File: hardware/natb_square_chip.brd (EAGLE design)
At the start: 13.5 x 13.5 mm, 8 parts, among them U1 TINY212, U2 MEGA32U4-MU

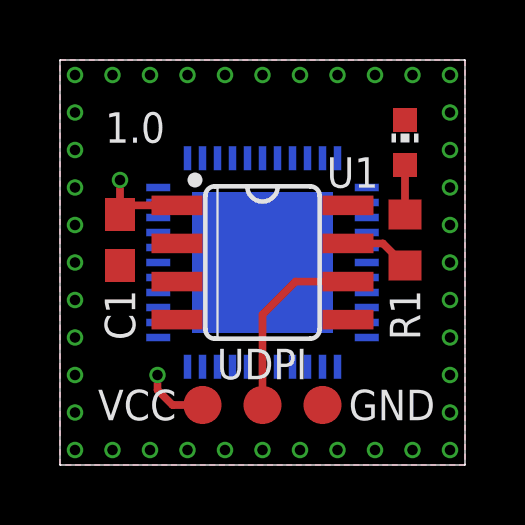
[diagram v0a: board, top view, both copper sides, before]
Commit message: Changes SOIC and BGA
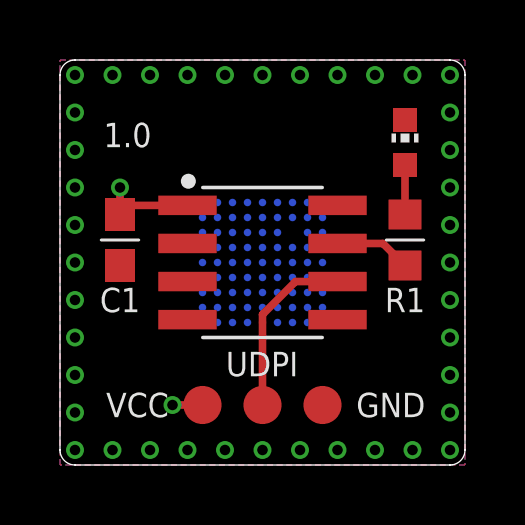
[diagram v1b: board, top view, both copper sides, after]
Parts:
- U2: value MEGA32U4-MU -> MSP432P401RIZXHR; device zaan-IC-Microcontroller:TQFN44_7MM -> Microcontroller:BGA80
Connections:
- removed net AREF: U2.42
- removed net AVCC: U2.24, U2.44
- removed net UCAP: U2.6
- removed net UGND: U2.5
- removed net UVCC: U2.2
- removed net VBUS: U2.7
- new net AVCC1: U2.F6
- new net AVCC2: U2.D5
- new net AVSS1: U2.F5
- new net AVSS2: U2.D6
- new net AVSS3: U2.E5
- new net DCOR: U2.J8
- new net DVCC1: U2.D2
- new net DVCC2: U2.C6
- new net DVSS1: U2.F2
- new net DVSS2: U2.E6
- new net DVSS3: U2.C7
- new net VCORE: U2.C2
- new net VSW: U2.E2
- net GND: no longer U2.15, U2.23, U2.35, U2.43, U2.EXP
- net VCC: no longer U2.14, U2.34
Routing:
- net VCC: track 5.38 -> 4.28 mm
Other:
- outline, holes or cut-outs redrawn
- board text added: "MSP432P401RIZX"
- board text removed: "ATmega32u4"

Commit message: Changed parts and added qr code
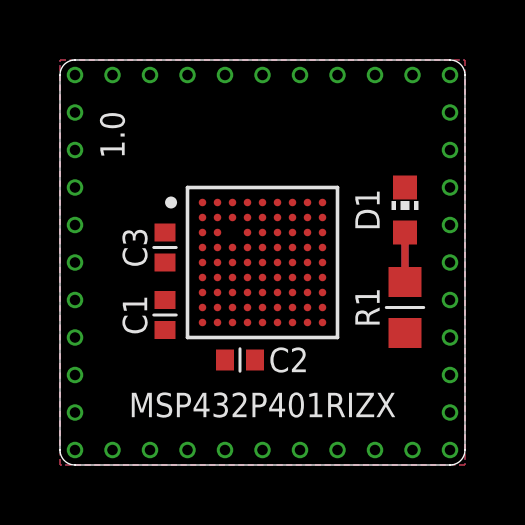
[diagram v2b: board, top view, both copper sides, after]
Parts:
- removed GND, UDPI, VCC: PTR1B1,27, testpad:B1,27
- removed LED1: (no value), led:CHIP-LED0603
- removed U1: TINY212, zaan-IC-Microcontroller:SO8
- added C2, C3: 22n, zaan-Capacitors:C0402
- added D1: (no value), led:CHIP-LED0603
- added U$1: (no value), zaan-Symbols:QR-NATB-10
- C1: value 10n -> 22n; device zaan-Capacitors:C0603 -> zaan-Capacitors:C0402
- moved C1 2.92 mm to (3.50, 5.00)
- moved R1 2.25 mm to (11.5, 5.25)
- flipped U2 to the top
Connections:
- removed net DVCC1: U2.D2
- removed net DVCC2: U2.C6
- removed net DVSS1: U2.F2
- removed net DVSS2: U2.E6
- removed net DVSS3: U2.C7
- removed net UDPI: U1.6, UDPI.TP
- removed net VCORE: U2.C2
- new net P1.0: U2.A1
- new net P1.1: U2.B1
- new net P1.2: U2.C4
- new net P1.3: U2.D4
- new net P1.4: U2.D3
- new net P1.5: U2.C1
- new net P1.6: U2.D1
- new net P1.7: U2.E1
- new net P2.0: U2.E4
- new net P2.1: U2.F1
- new net P2.2: U2.E3
- new net P2.3: U2.F4
- new net P2.4: U2.F3
- new net P2.5: U2.G1
- new net P2.6: U2.G2
- new net P2.7: U2.H1
- new net P3.0: U2.J3
- new net P3.1: U2.H4
- new net P3.2: U2.G5
- new net P3.3: U2.J4
- new net P3.4: U2.H5
- new net P3.5: U2.G6
- new net P3.6: U2.J5
- new net P3.7: U2.H6
- new net P4.0: U2.H9
- new net P4.1: U2.H8
- new net P4.2: U2.G7
- new net P4.3: U2.G8
- new net P4.4: U2.G9
- new net P4.5: U2.F7
- new net P4.6: U2.F8
- new net P4.7: U2.F9
- new net P5.0: U2.E7
- new net P5.1: U2.E8
- new net P5.2: U2.E9
- new net P5.3: U2.D7
- new net P5.4: U2.D8
- new net P5.5: U2.C8
- new net P5.6: U2.D9
- new net P5.7: U2.C9
- new net P6.0: U2.J9
- new net P6.1: U2.H7
- new net P6.2: U2.A9
- new net P6.3: U2.B9
- new net P6.4: U2.A8
- new net P6.5: U2.A7
- new net P6.6: U2.B8
- new net P6.7: U2.B7
- new net P7.0: U2.B5
- new net P7.1: U2.C5
- new net P7.2: U2.B4
- new net P7.3: U2.A4
- new net P7.4: U2.J1
- new net P7.5: U2.H2
- new net P7.6: U2.J2
- new net P7.7: U2.G3
- new net P8.0: U2.H3
- new net P8.1: U2.G4
- new net PJ.0: U2.J6
- new net PJ.1: U2.J7
- new net PJ.2: U2.A6
- new net PJ.3: U2.A5
- new net PJ.4: U2.B3
- new net PJ.5: U2.A3
- new net RSTN/NMI: U2.B6
- new net SWCLKTCK: U2.A2
- new net SWDIOTMS: U2.B2
- net GND: now also C2.2, C3.2, D1.C, U2.C7, U2.E6, U2.F2; no longer GND.TP, LED1.C, U1.8
- net LED: no longer U1.7
- net N$1: now also D1.A; no longer LED1.A
- net VCC: now also C2.1, C3.1, U2.C2, U2.C6, U2.D2; no longer U1.1, VCC.TP
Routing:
- net UDPI: track 5.97 -> 0.00 mm
- net VCC: track 4.28 -> 0.00 mm, vias 2 -> 0
- net LED: track 2.55 -> 0.00 mm
